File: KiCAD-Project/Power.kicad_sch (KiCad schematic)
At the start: 19 parts, among them U401 DRV8323SRTAR-DRV8323SRTAR

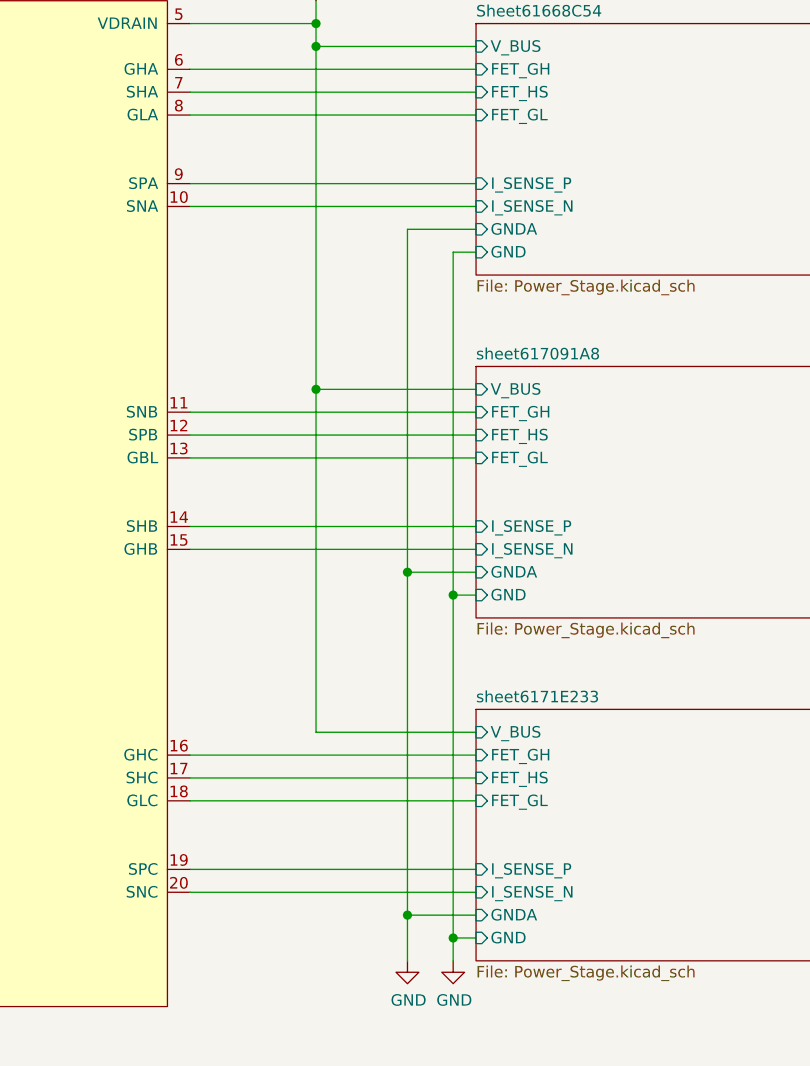
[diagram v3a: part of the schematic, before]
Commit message: minor pcb updates
swapped Encoder Quadrature signals, to provide debug UART
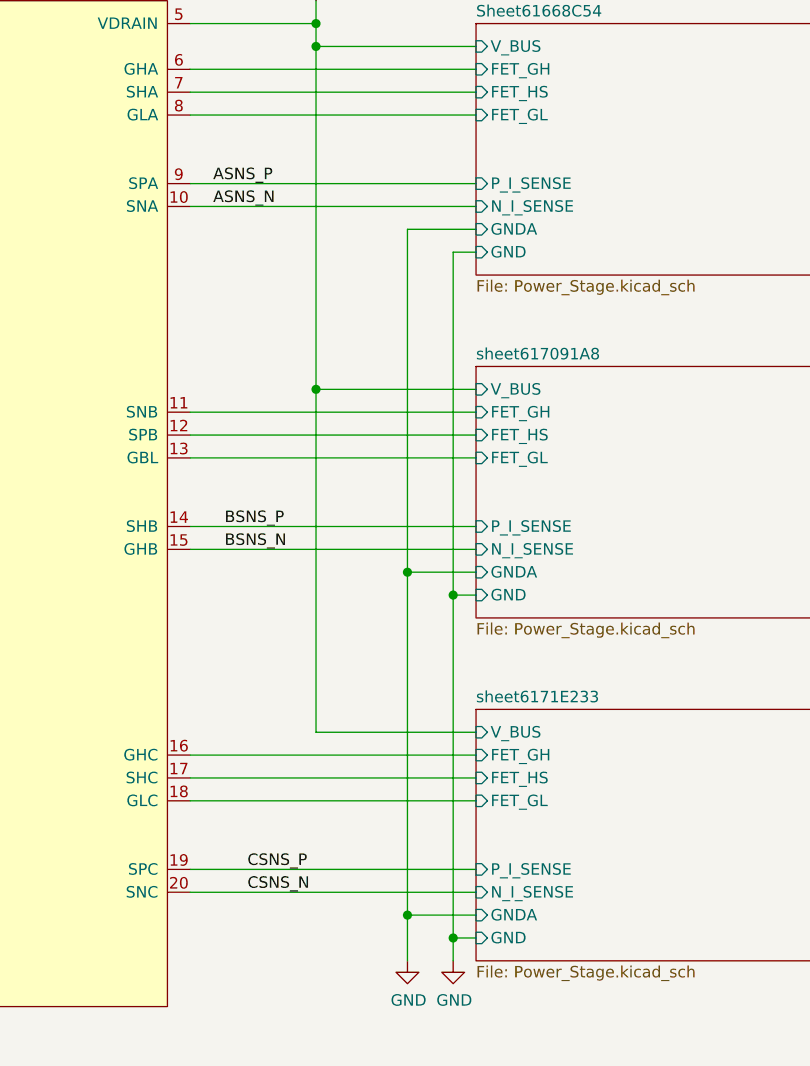
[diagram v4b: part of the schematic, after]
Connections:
- net Sheet61668C54/I_SENSE_N renamed ASNS_N
- net Sheet61668C54/I_SENSE_P renamed ASNS_P
- net sheet617091A8/I_SENSE_N renamed BSNS_N
- net sheet617091A8/I_SENSE_P renamed BSNS_P
- net sheet6171E233/I_SENSE_N renamed CSNS_N
- net sheet6171E233/I_SENSE_P renamed CSNS_P
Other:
- sheet Sheet61668C54 ports: added N_I_SENSE, P_I_SENSE; removed I_SENSE_N, I_SENSE_P
- sheet sheet617091A8 ports: added N_I_SENSE, P_I_SENSE; removed I_SENSE_N, I_SENSE_P
- sheet sheet6171E233 ports: added N_I_SENSE, P_I_SENSE; removed I_SENSE_N, I_SENSE_P
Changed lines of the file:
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@@
     (stroke (width 0) (type solid) (color 0 0 0 0))
+  )
+  (label "ASNS_P" (at 190.5 55.88 0)
+    (effects (font (size 1.27 1.27)) (justify left bottom))
+  )
+  (label "ASNS_N" (at 190.5 58.42 0)
+    (effects (font (size 1.27 1.27)) (justify left bottom))
+  )
+  (label "BSNS_P" (at 191.77 93.98 0)
+    (effects (font (size 1.27 1.27)) (justify left bottom))
+  )
+  (label "BSNS_N" (at 191.77 96.52 0)
+    (effects (font (size 1.27 1.27)) (justify left bottom))
+  )
+  (label "CSNS_P" (at 194.31 132.08 0)
+    (effects (font (size 1.27 1.27)) (justify left bottom))
+  )
+  (label "CSNS_N" (at 194.31 134.62 0)
+    (effects (font (size 1.27 1.27)) (justify left bottom))
   )
   (hierarchical_label "DRV_PWM_AL" (shape input) (at 76.2 81.28 180)
@@
       (effects (font (size 1.27 1.27)) (justify left))
     )
-    (pin "I_SENSE_N" input (at 219.71 58.42 180)
-      (effects (font (size 1.27 1.27)) (justify left))
-    )
-    (pin "I_SENSE_P" input (at 219.71 55.88 180)
+    (pin "N_I_SENSE" input (at 219.71 58.42 180)
+      (effects (font (size 1.27 1.27)) (justify left))
+    )
+    (pin "P_I_SENSE" input (at 219.71 55.88 180)
       (effects (font (size 1.27 1.27)) (justify left))
     )
@@
       (effects (font (size 1.27 1.27)) (justify left))
     )
-    (pin "I_SENSE_N" input (at 219.71 96.52 180)
-      (effects (font (size 1.27 1.27)) (justify left))
-    )
-    (pin "I_SENSE_P" input (at 219.71 93.98 180)
-      (effects (font (size 1.27 1.27)) (justify left))
-    )
     (pin "FET_GH" input (at 219.71 81.28 180)
       (effects (font (size 1.27 1.27)) (justify left))
@@
     )
     (pin "GNDA" input (at 219.71 99.06 180)
+      (effects (font (size 1.27 1.27)) (justify left))
+    )
+    (pin "P_I_SENSE" input (at 219.71 93.98 180)
+      (effects (font (size 1.27 1.27)) (justify left))
+    )
+    (pin "N_I_SENSE" input (at 219.71 96.52 180)
       (effects (font (size 1.27 1.27)) (justify left))
     )
@@
       (effects (font (size 1.27 1.27)) (justify left))
     )
-    (pin "I_SENSE_N" input (at 219.71 134.62 180)
-      (effects (font (size 1.27 1.27)) (justify left))
-    )
-    (pin "I_SENSE_P" input (at 219.71 132.08 180)
-      (effects (font (size 1.27 1.27)) (justify left))
-    )
     (pin "FET_GH" input (at 219.71 119.38 180)
       (effects (font (size 1.27 1.27)) (justify left))
@@
       (effects (font (size 1.27 1.27)) (justify left))
     )
+    (pin "P_I_SENSE" input (at 219.71 132.08 180)
+      (effects (font (size 1.27 1.27)) (justify left))
+    )
+    (pin "N_I_SENSE" input (at 219.71 134.62 180)
+      (effects (font (size 1.27 1.27)) (justify left))
+    )
